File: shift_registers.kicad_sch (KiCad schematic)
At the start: 8 parts, among them U1 IC_HV5622PG-G, U2 IC_HV5622PG-G

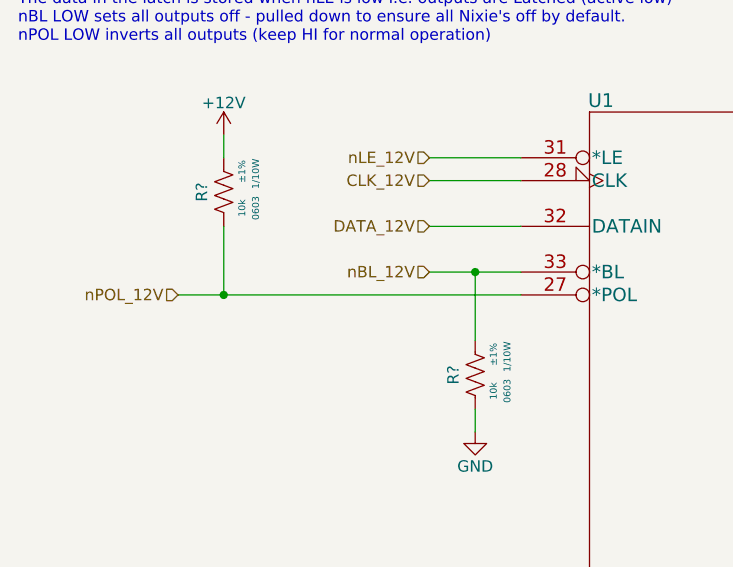
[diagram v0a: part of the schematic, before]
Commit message: Added USBC Connector to power page
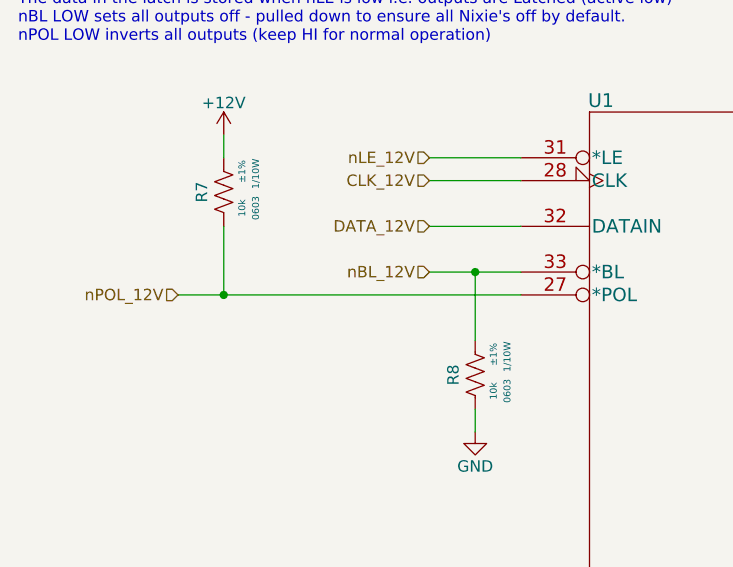
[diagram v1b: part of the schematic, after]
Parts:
- gave numbers to parts that had none: 2
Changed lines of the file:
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@@
   (symbol (lib_id "arjun_symbols:RES_10K_1P_1{slash}10W_0603") (at 66.04 58.42 0) (unit 1)
     (in_bom yes) (on_board yes)
-    (property "Reference" "R?" (id 0) (at 62.865 62.23 90)
+    (property "Reference" "R8" (id 0) (at 62.865 62.23 90)
       (effects (font (size 1.27 1.27)) (justify top))
     )
@@
   (symbol (lib_id "power:GND") (at 66.04 68.58 0) (unit 1)
     (in_bom yes) (on_board yes)
-    (property "Reference" "#PWR?" (id 0) (at 66.04 74.93 0)
+    (property "Reference" "#PWR013" (id 0) (at 66.04 74.93 0)
       (effects (font (size 1.27 1.27)) hide)
     )
@@
   (symbol (lib_id "power:+12V") (at 38.1 35.56 0) (unit 1)
     (in_bom yes) (on_board yes)
-    (property "Reference" "#PWR?" (id 0) (at 38.1 39.37 0)
+    (property "Reference" "#PWR012" (id 0) (at 38.1 39.37 0)
       (effects (font (size 1.27 1.27)) hide)
     )
@@
   (symbol (lib_id "arjun_symbols:RES_10K_1P_1{slash}10W_0603") (at 38.1 38.1 0) (unit 1)
     (in_bom yes) (on_board yes)
-    (property "Reference" "R?" (id 0) (at 34.925 41.91 90)
+    (property "Reference" "R7" (id 0) (at 34.925 41.91 90)
       (effects (font (size 1.27 1.27)) (justify top))
     )
